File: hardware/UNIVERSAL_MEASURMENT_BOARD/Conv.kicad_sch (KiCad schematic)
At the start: 99 parts, among them U10 L7805ABD2T-TR, U11 L7812ABD2T-TR, U12 L78L15ACD13TR, U13 L79L15ACD13TR, U14 ISL21010CFH315Z-TK, U15 ISL21010CFH330Z-TK, U5 TPS54202HDDCR, U6 TPS54202HDDCR, U7 LT3471EDD#PBF, U8 UA78M33CDCYRG3, U9 UA78M33CDCYRG3

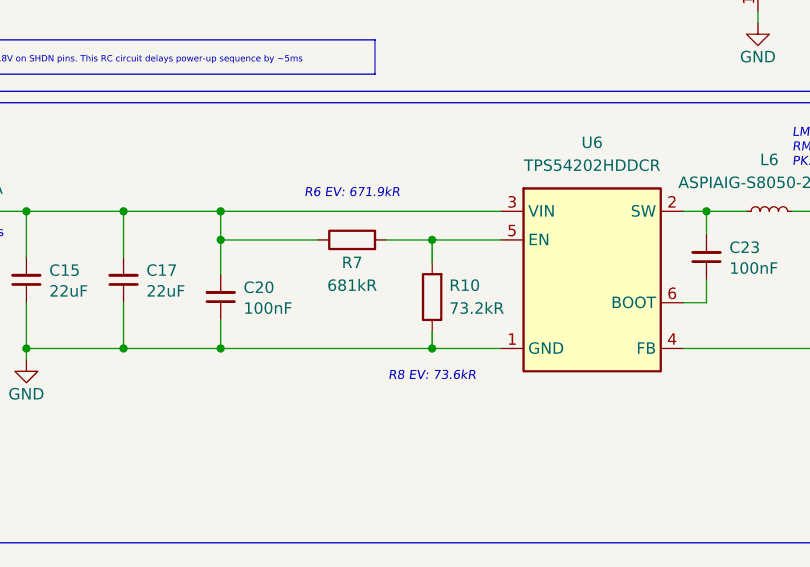
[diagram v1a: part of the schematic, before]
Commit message: Fixed VOUT range of PGA to 3.0V, fixed GPIO connection between FDCAN and MCU, added 1.5V VREF to PGA, changed value of enable divider of 7V DCDC converter.
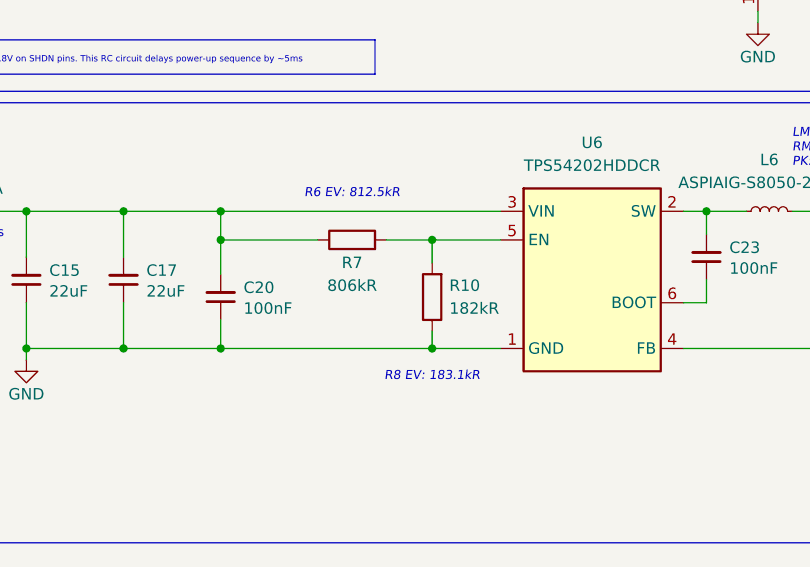
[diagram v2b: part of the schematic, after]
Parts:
- R10: value 73.2kR -> 182kR
- R7: value 681kR -> 806kR
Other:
- note added: "R6 EV: 812.5kR"
- note added: "R8 EV: 183.1kR"
- note removed: "R6 EV: 671.9kR"
- note removed: "R8 EV: 73.6kR"
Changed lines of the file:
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@@
 (kicad_sch
-	(version 20260101)
+	(version 20260306)
 	(generator "eeschema")
 	(generator_version "10.0")
@@
 		(title "Universal Measurment Board")
 		(date "2026-03-26")
-		(rev "1.9.21")
+		(rev "1.11.22")
 		(company "PUT Motorsport Formula Student Team")
 		(comment 1 "Designed by Marcin Trzmiel under")
@@
 		)
 	)
-	(text "R6 EV: 671.9kR"
+	(text "R6 EV: 812.5kR"
 		(exclude_from_sim no)
 		(at 85.725 172.72 0)
@@
 		)
 	)
-	(text "R8 EV: 73.6kR"
+	(text "R8 EV: 183.1kR"
 		(exclude_from_sim no)
 		(at 94.615 193.04 0)
@@
 			)
 		)
-		(property "Value" "73.2kR"
+		(property "Value" "182kR"
 			(at 96.52 185.42 0)
 			(show_name no)
@@
 			)
 		)
-		(property "Value" "681kR"
+		(property "Value" "806kR"
 			(at 85.725 182.88 90)
 			(show_name no)

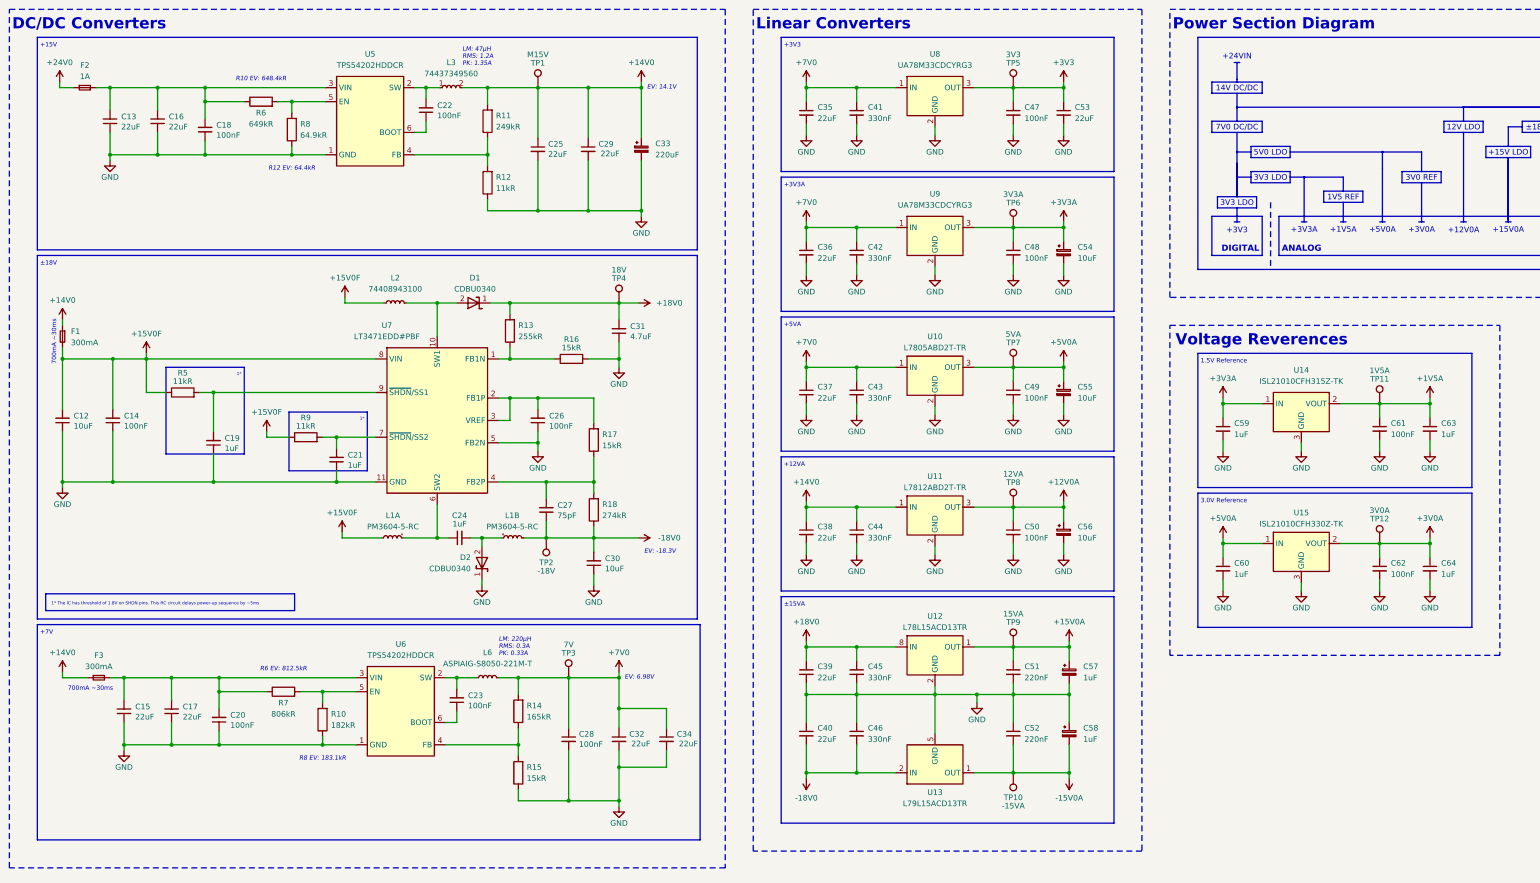
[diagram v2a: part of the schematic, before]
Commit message: Reduced PCB dimensions, working on power section
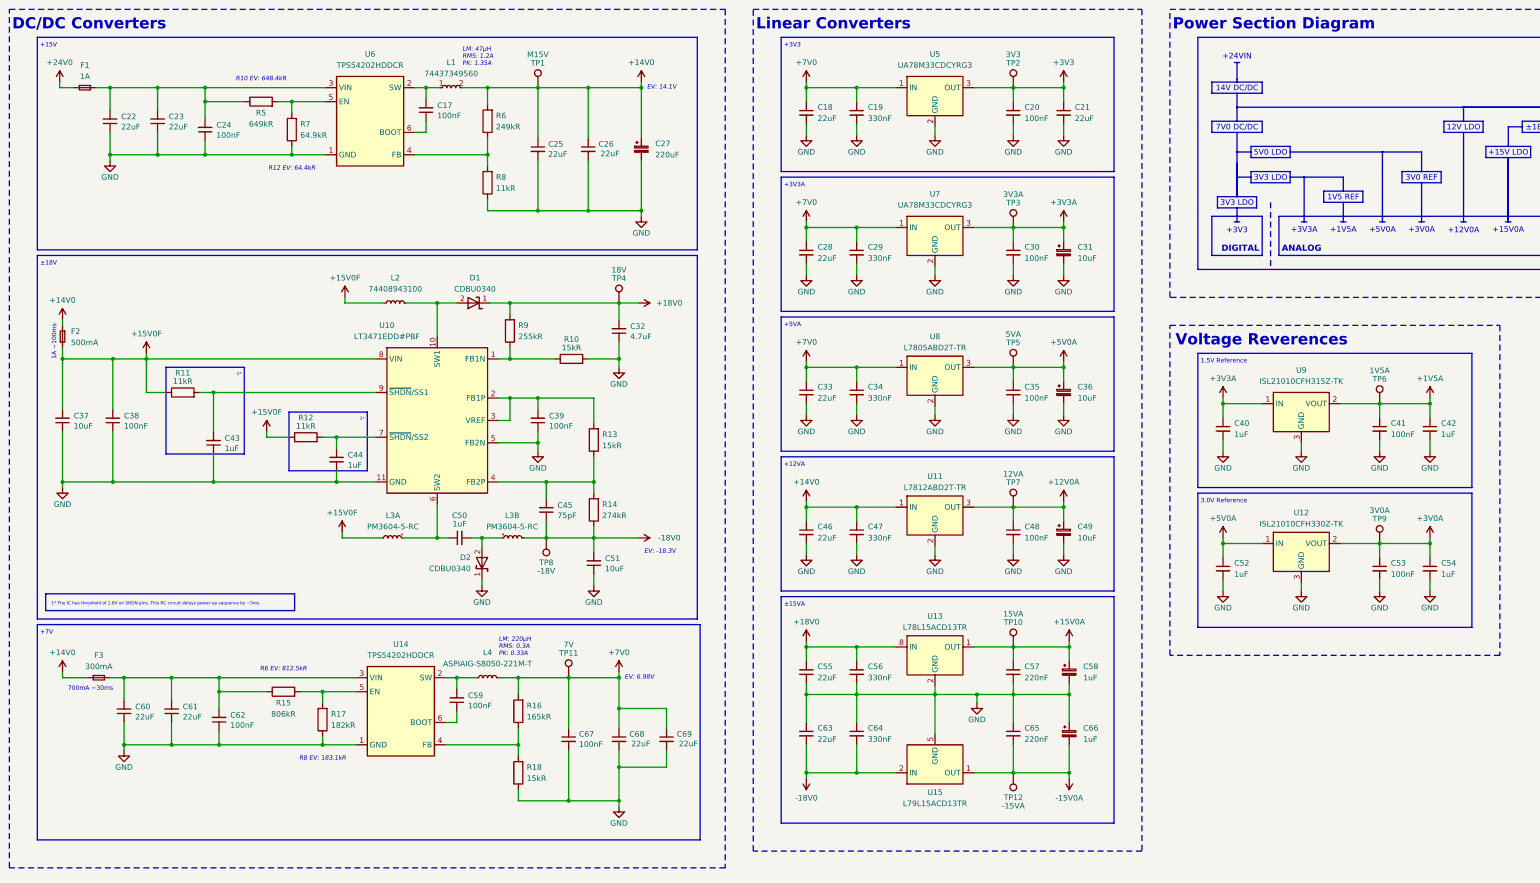
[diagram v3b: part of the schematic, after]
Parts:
- F2: renamed from F1; value 300mA -> 500mA
- renumbered C22 to C17, C35 to C18, C41 to C19, C47 to C20, C53 to C21, C13 to C22, C16 to C23, C18 to C24, C29 to C26, C33 to C27, C36 to C28, C42 to C29, C48 to C30, C54 to C31, C31 to C32, C37 to C33, C43 to C34, C49 to C35, C55 to C36, C12 to C37, C14 to C38, C26 to C39, C59 to C40, C61 to C41, C63 to C42, C19 to C43, C21 to C44, C27 to C45, C38 to C46, C44 to C47, C50 to C48, C56 to C49, C24 to C50, C30 to C51, C60 to C52, C62 to C53, C64 to C54, C39 to C55, C45 to C56, C51 to C57, C57 to C58, C23 to C59, C15 to C60, C17 to C61, C20 to C62, C40 to C63, C46 to C64, C52 to C65, C58 to C66, C28 to C67, C32 to C68, C34 to C69, F2 to F1, L3 to L1, L1 to L3, L6 to L4, R16 to R10, R5 to R11, R9 to R12, R17 to R13, R18 to R14, R7 to R15, R14 to R16, R10 to R17, R15 to R18, R6 to R5, R11 to R6, R8 to R7, R12 to R8, R13 to R9, TP9 to TP10, TP3 to TP11, TP10 to TP12, TP5 to TP2, TP6 to TP3, TP7 to TP5, TP11 to TP6, TP8 to TP7, TP2 to TP8, TP12 to TP9, U7 to U10, U15 to U12, U12 to U13, U6 to U14, U13 to U15, U8 to U5, U5 to U6, U9 to U7, U10 to U8, U14 to U9
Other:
- note added: "1A ~100ms"
